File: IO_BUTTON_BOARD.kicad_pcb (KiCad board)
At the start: 2 copper layers, 113 parts, among them P1 I2C, P10 IO_7, P2 I2C, P3 IO_0, P4 IO_1, P5 IO_2, P6 IO_3, P7 IO_4, P8 IO_5, P9 IO_6, Q1 NPN, Q10 PNP, Q11 PNP, Q12 PNP, Q13 PNP, Q2 PNP, Q3 NPN, Q4 PNP, Q5 NPN, Q6 PNP, Q7 PNP, Q8 PNP, Q9 PNP, SW1 I2C_ADDR, SW2 SW_0, SW3 SW_1, SW4 SW_2, SW5 SW_3, SW6 SW_4, SW7 SW_5, SW8 SW_6, SW9 SW_7, U1 PCF8574A, U2 74HC86, U3 74HC86

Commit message: Fix footprint for Q13 Place components on board
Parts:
- Q10, Q11, Q12, Q6, Q7, Q8, Q9, R11, R12, R13, R14, R15, R16, R17, R18, R19, R20, R21, R22, R23, R24, R25, R26, R27, R28, R29, R30, R31, R32, R33, R34, R35, R36, R37, R38, R39, R40, R41, R42, R43, R44, R45, R46, R47, R48, R49, R50, U2, U3: moved to B.Cu
- Q13: footprint Resistors_SMD:R_0805 -> TO_SOT_Packages_SMD:SOT-23; moved to B.Cu
- moved U3 182.3 mm to (91.3, 36.7), turned to 180 degrees
- moved R32 181.8 mm to (78.6, 46.8)
- moved P10 178.6 mm to (134.6, 48.3)
- moved P3 178.6 mm to (99.1, 48.3)
- moved P4 178.6 mm to (104.1, 48.3)
- moved P5 178.6 mm to (109.2, 48.3)
- moved P6 178.6 mm to (114.3, 48.3)
- moved P7 178.6 mm to (119.4, 48.3)
- moved P8 178.6 mm to (124.5, 48.3)
- moved S1 178.6 mm to (99.1, 43.2)
- moved S2 178.6 mm to (104.1, 43.2)
- moved S3 178.6 mm to (109.2, 43.2)
- moved S4 178.6 mm to (114.3, 43.2)
- moved S5 178.6 mm to (119.4, 43.2)
- moved S6 178.6 mm to (124.5, 43.2)
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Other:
- board outline added: 80 x 40 mm

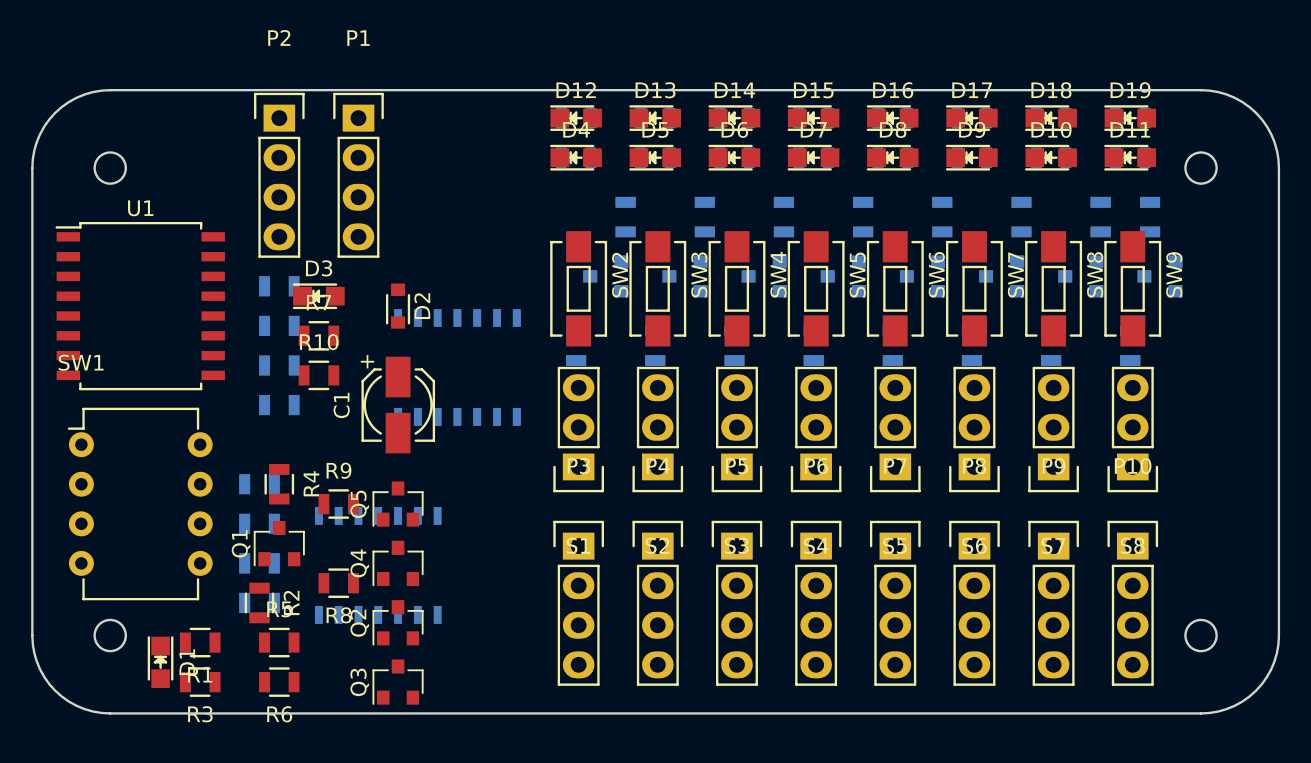
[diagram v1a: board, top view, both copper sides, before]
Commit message: First routed version of the pcb
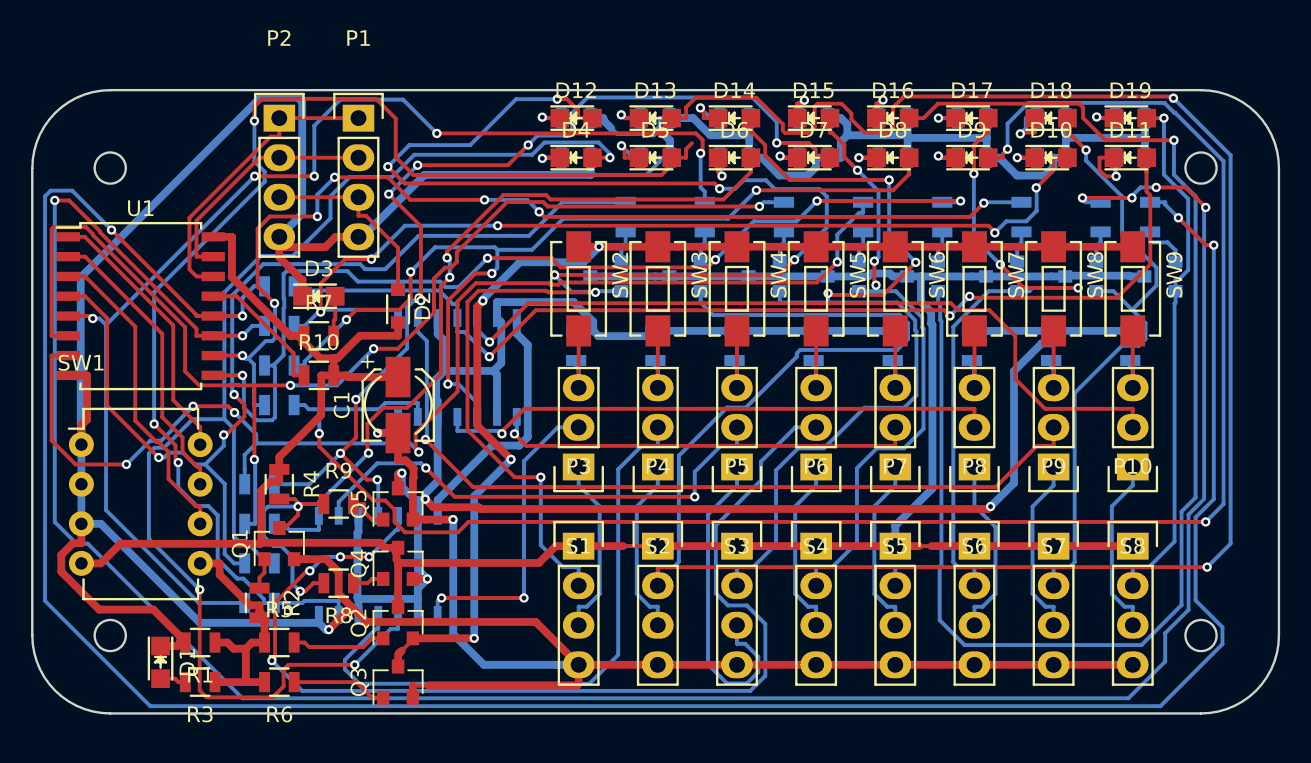
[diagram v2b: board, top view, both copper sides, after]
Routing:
- net GND: track 0.00 -> 276.7 mm, vias 0 -> 3
- net +5V: track 0.00 -> 164.0 mm
- net Net-(R27-Pad1): track 0.00 -> 157.2 mm, vias 0 -> 4
- net Net-(R28-Pad1): track 0.00 -> 155.5 mm, vias 0 -> 6
- net /OUT_1: track 0.00 -> 150.3 mm, vias 0 -> 2
- net /PULL_LANE: track 0.00 -> 134.4 mm, vias 0 -> 4
- net Net-(D9-Pad2): track 0.00 -> 114.2 mm, vias 0 -> 3
- net /OUT_0: track 0.00 -> 101.9 mm, vias 0 -> 7
- net /OUT_4: track 0.00 -> 92.0 mm, vias 0 -> 1
- net Net-(D4-Pad2): track 0.00 -> 89.2 mm, vias 0 -> 3
- net Net-(R31-Pad1): track 0.00 -> 77.9 mm, vias 0 -> 5
- net Net-(D5-Pad2): track 0.00 -> 77.8 mm, vias 0 -> 3
- net Net-(R33-Pad1): track 0.00 -> 77.3 mm, vias 0 -> 5
- net Net-(R32-Pad1): track 0.00 -> 77.2 mm, vias 0 -> 4
- net /CONTACT_LANE: track 0.00 -> 74.4 mm, vias 0 -> 4
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
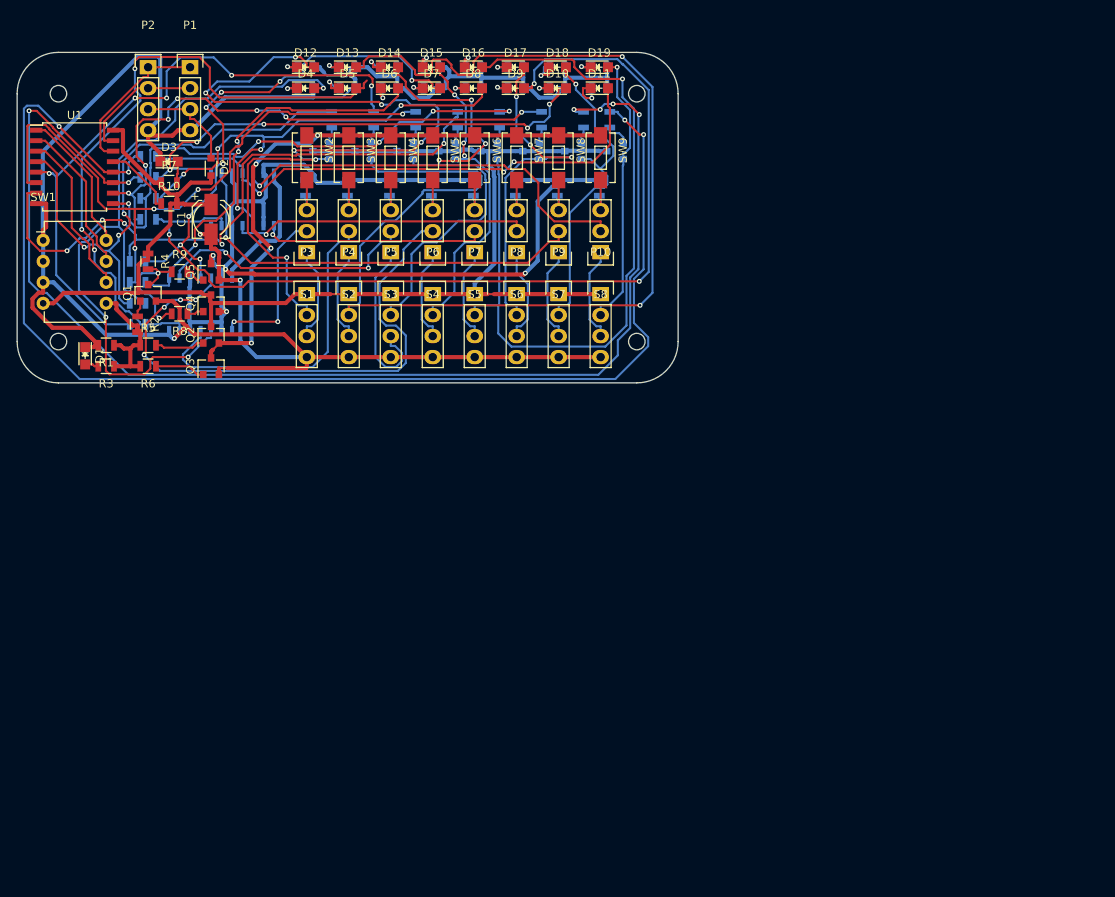
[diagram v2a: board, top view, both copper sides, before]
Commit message: Replace regular pins with molex KK connectors =>  - replace connectors  - reroute the pcb
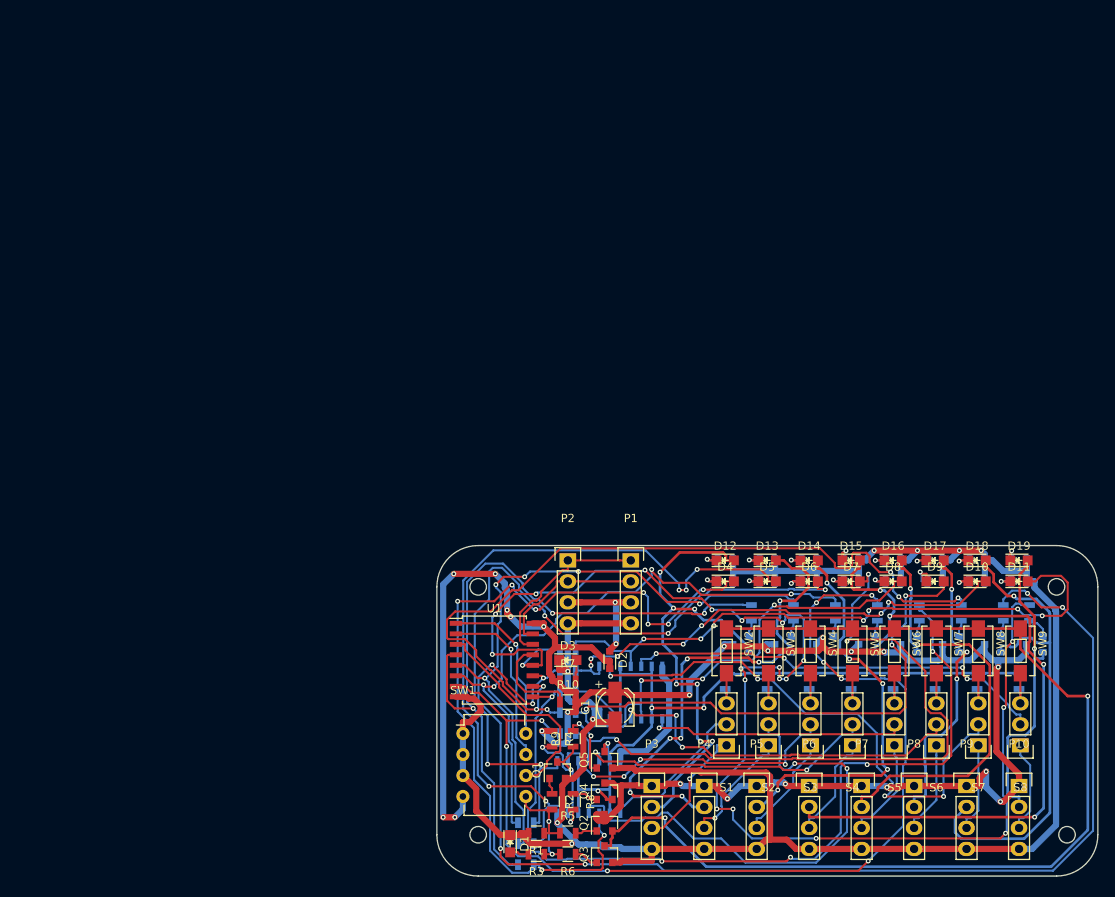
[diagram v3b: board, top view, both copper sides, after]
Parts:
- moved R34 82.6 mm to (125.6, 117.3)
- moved R32 80.5 mm to (125.6, 112.2)
- moved P1 80.1 mm to (138.3, 80.5)
- moved R1 78.7 mm to (126.8, 113.5)
- moved R3 78.7 mm to (126.8, 116.0)
- moved R33 78.5 mm to (125.6, 114.8)
- moved D10 78.4 mm to (180.2, 83.0)
- moved D6 78.4 mm to (159.9, 83.0)
- moved D8 78.4 mm to (170.0, 83.0)
- moved R13 78.4 mm to (159.9, 83.0)
- moved R15 78.4 mm to (170.0, 83.0)
- moved R17 78.4 mm to (180.2, 83.0)
- moved R29 78.4 mm to (130.7, 98.9)
- moved R45 78.4 mm to (159.9, 95.1)
- moved R47 78.4 mm to (170.0, 95.1)
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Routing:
- net /OUT_1: track 150.3 -> 60.7 mm, vias 2 -> 7
- net +5V: track 164.0 -> 237.6 mm, vias 0 -> 22
- net /CONTACT_LANE: track 74.4 -> 130.4 mm, vias 4 -> 2
- net /OUT_3: track 39.1 -> 88.0 mm, vias 3 -> 4
- net Net-(R31-Pad1): track 77.9 -> 126.4 mm, vias 5 -> 8
- net Net-(D9-Pad2): track 114.2 -> 67.1 mm
- net Net-(D6-Pad2): track 48.2 -> 91.3 mm, vias 3 -> 5
- net Net-(R30-Pad1): track 64.5 -> 105.7 mm
- net /OUT_0: track 101.9 -> 61.0 mm
- net /PULL_LANE: track 134.4 -> 94.2 mm
- net /OUT_4: track 92.0 -> 51.9 mm, vias 1 -> 2
- net Net-(S4-Pad2): track 68.8 -> 36.5 mm, vias 4 -> 2
- net Net-(R29-Pad1): track 68.5 -> 98.2 mm, vias 7 -> 6
- net Net-(R34-Pad1): track 64.9 -> 86.5 mm
- net Net-(S2-Pad2): track 39.4 -> 60.9 mm, vias 0 -> 2
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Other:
- outline, holes or cut-outs redrawn

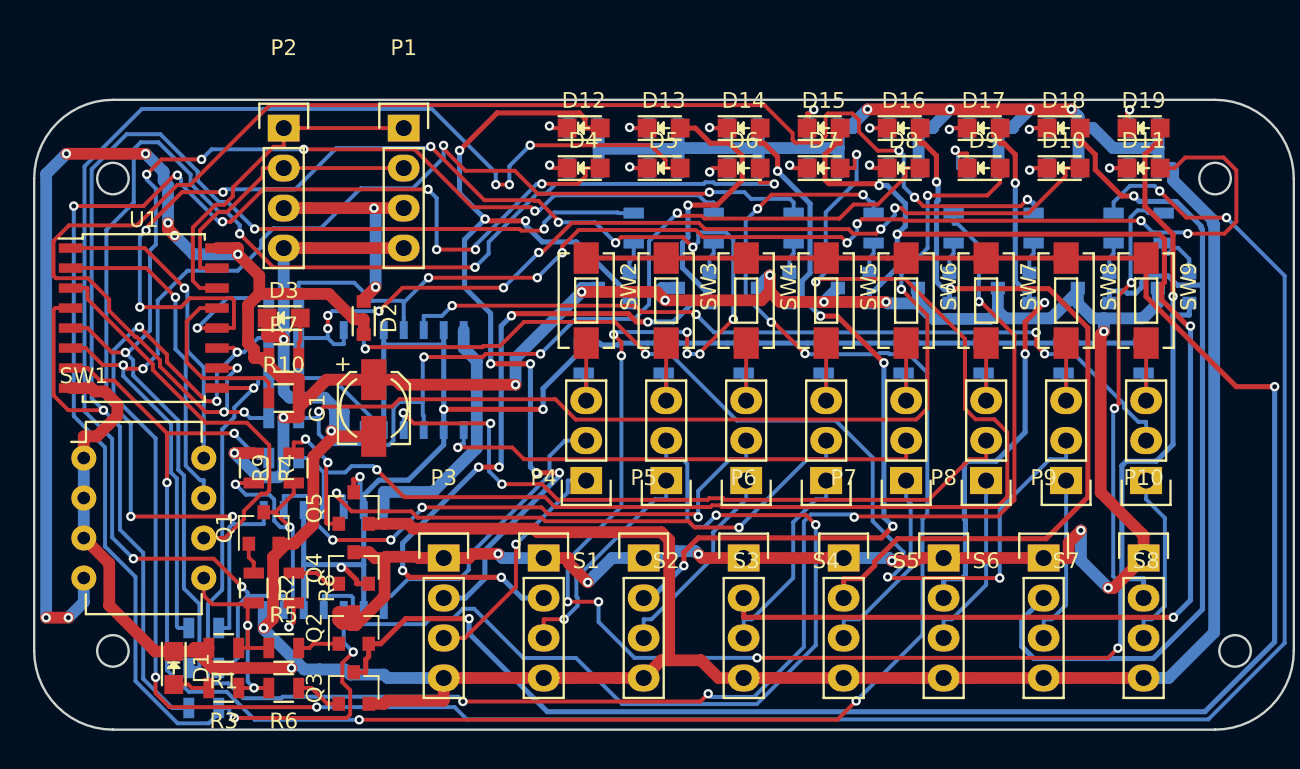
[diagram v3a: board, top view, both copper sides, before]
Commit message: Change silk-screening of the PCB
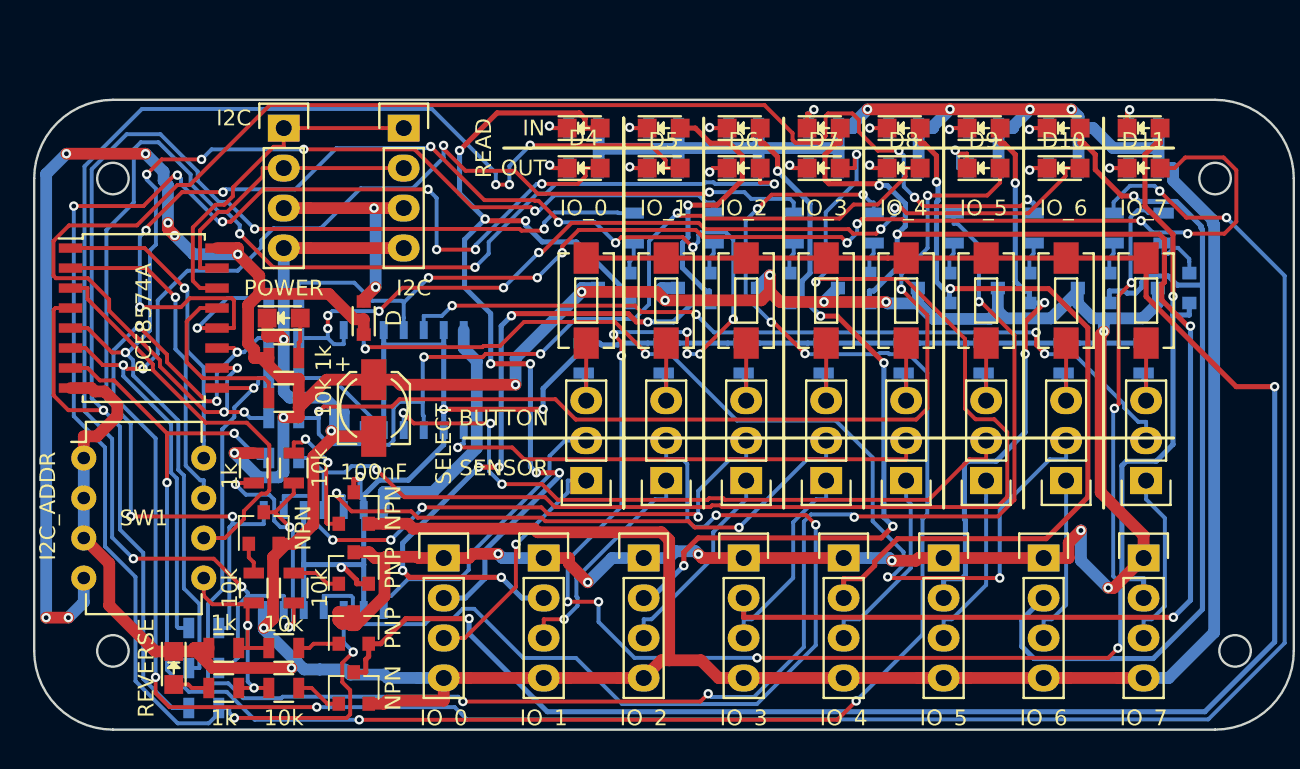
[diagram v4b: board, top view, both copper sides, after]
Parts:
- C1: value 100n -> 100nF
- D10: value IN_6 -> IO_6
- D11: value IN_7 -> IO_7
- D4: value IN_0 -> IO_0
- D5: value IN_1 -> IO_1
- D6: value IN_2 -> IO_2
- D7: value IN_3 -> IO_3
- D8: value IN_4 -> IO_4
- D9: value IN_5 -> IO_5
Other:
- board text added: "BUTTON"
- board text added: "IN"
- board text added: "OUT"
- board text added: "READ"
- board text added: "SELECT"
- board text added: "SENSOR"
